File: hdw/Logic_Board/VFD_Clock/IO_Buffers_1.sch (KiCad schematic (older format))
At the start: 42 parts

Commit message: Resurrected project
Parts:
- removed R? (x16): 100, Resistors_SMD:R_0603, symbol Custom_Library:R_Custom
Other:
- note added: "Switch to nexperia QFN line driver"

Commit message: Power supply additions
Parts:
- removed R? (x16): 10K, Resistors_SMD:R_0603, symbol Custom_Library:R_Custom
- removed U? (x2): 74HCT541, Housings_SSOP:TSSOP-20_4.4x6.5mm_Pitch0.65mm, symbol 74xx:74HCT541
- added RN? (x2): 10k, Resistors_SMD:R_Array_Convex_8x0602, symbol Device:R_Pack08
- added U? (x2): 74VHC541, Package_DFN_QFN:Texas_S-PWQFN-N20, symbol Custom_Library:74VHC541
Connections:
- wire segments 84 -> 118
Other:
- note removed: "Switch to nexperia QFN line driver"

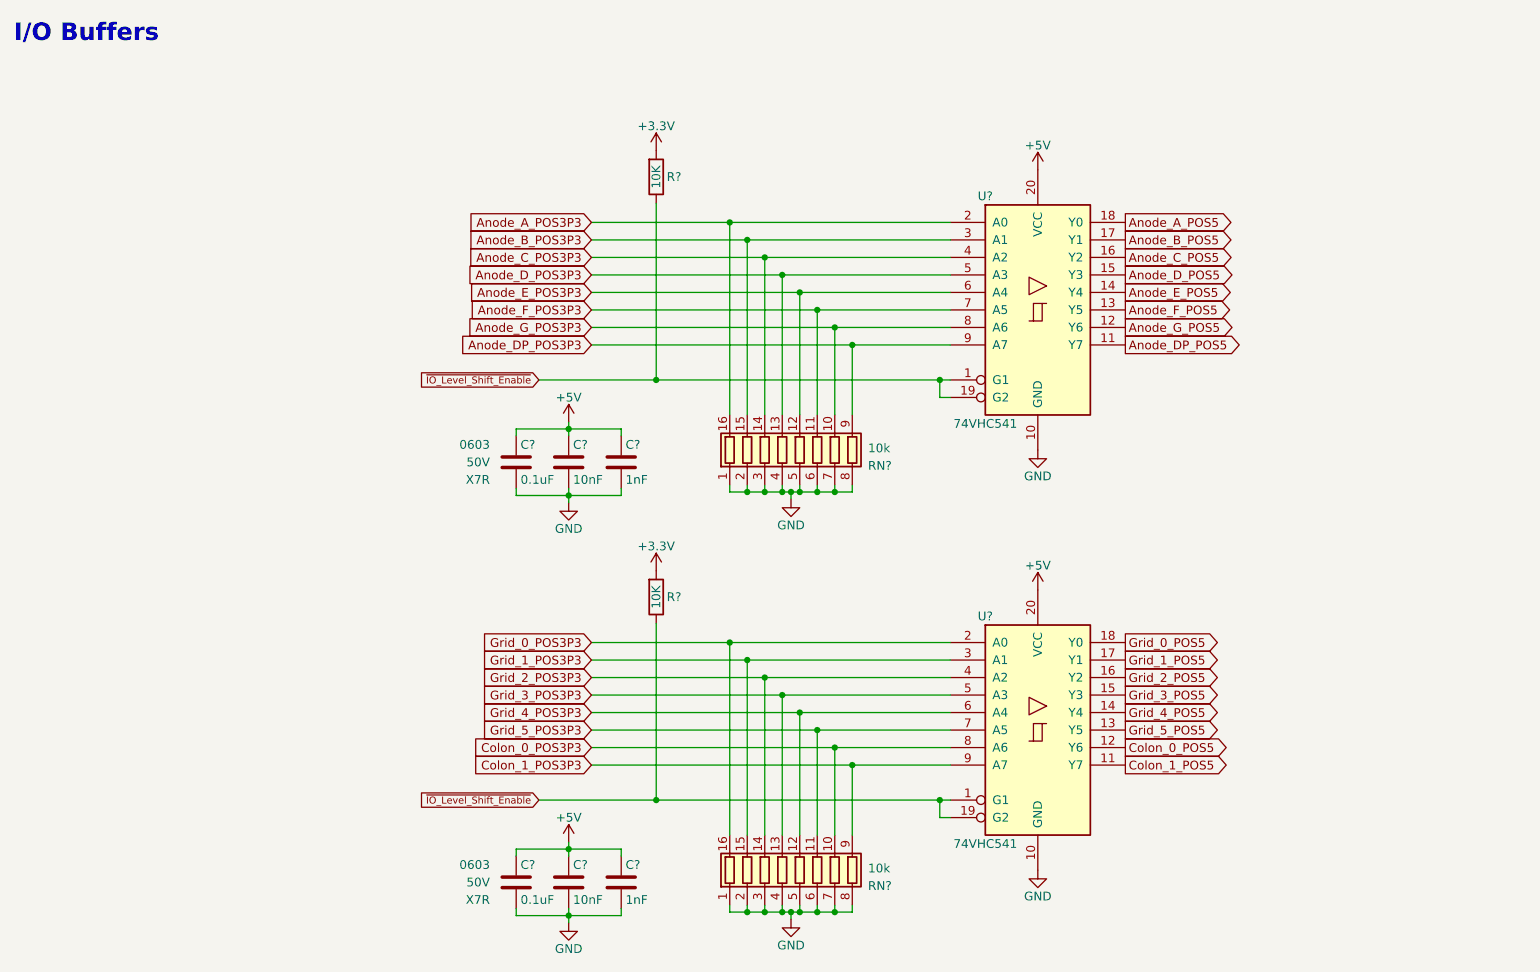
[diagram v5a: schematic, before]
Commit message: Started IV-6 display board, continued logic board development
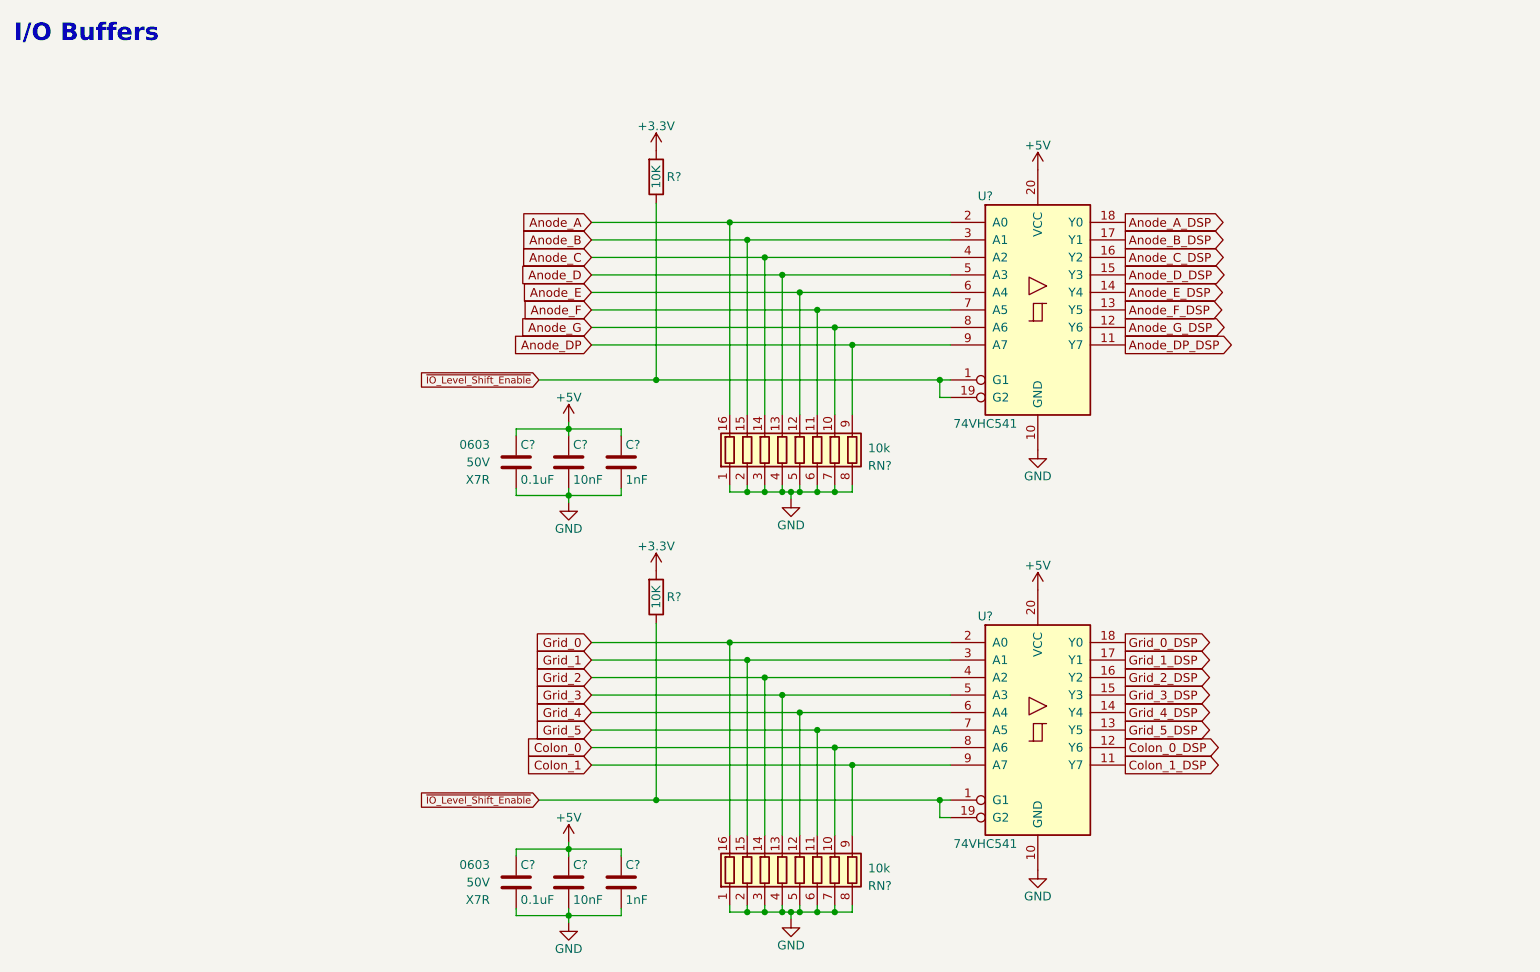
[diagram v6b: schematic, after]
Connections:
- net Anode_A_POS3P3 renamed Anode_A
- net Anode_A_POS5 renamed Anode_A_DSP
- net Anode_B_POS3P3 renamed Anode_B
- net Anode_B_POS5 renamed Anode_B_DSP
- net Anode_C_POS3P3 renamed Anode_C
- net Anode_C_POS5 renamed Anode_C_DSP
- net Anode_DP_POS3P3 renamed Anode_DP
- net Anode_DP_POS5 renamed Anode_DP_DSP
- net Anode_D_POS3P3 renamed Anode_D
- net Anode_D_POS5 renamed Anode_D_DSP
- net Anode_E_POS3P3 renamed Anode_E
- net Anode_E_POS5 renamed Anode_E_DSP
- net Anode_F_POS3P3 renamed Anode_F
- net Anode_F_POS5 renamed Anode_F_DSP
- net Anode_G_POS3P3 renamed Anode_G
- net Anode_G_POS5 renamed Anode_G_DSP
- net Colon_0_POS3P3 renamed Colon_0
- net Colon_0_POS5 renamed Colon_0_DSP
- net Colon_1_POS3P3 renamed Colon_1
- net Colon_1_POS5 renamed Colon_1_DSP
- net Grid_0_POS3P3 renamed Grid_0
- net Grid_0_POS5 renamed Grid_0_DSP
- net Grid_1_POS3P3 renamed Grid_1
- net Grid_1_POS5 renamed Grid_1_DSP
- net Grid_2_POS3P3 renamed Grid_2
- net Grid_2_POS5 renamed Grid_2_DSP
- net Grid_3_POS3P3 renamed Grid_3
- net Grid_3_POS5 renamed Grid_3_DSP
- net Grid_4_POS3P3 renamed Grid_4
- net Grid_4_POS5 renamed Grid_4_DSP
- net Grid_5_POS3P3 renamed Grid_5
- net Grid_5_POS5 renamed Grid_5_DSP
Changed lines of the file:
@@
 Connection ~ 5840 5020
 Text GLabel 3850 1720 0    50   Input ~ 0
-Anode_A_POS3P3
+Anode_A
 Text GLabel 3850 1820 0    50   Input ~ 0
-Anode_B_POS3P3
+Anode_B
 Text GLabel 3850 1920 0    50   Input ~ 0
-Anode_C_POS3P3
+Anode_C
 Text GLabel 3850 2020 0    50   Input ~ 0
-Anode_D_POS3P3
+Anode_D
 Text GLabel 3850 2120 0    50   Input ~ 0
-Anode_E_POS3P3
+Anode_E
 Text GLabel 3850 2220 0    50   Input ~ 0
-Anode_F_POS3P3
+Anode_F
 Text GLabel 3850 2320 0    50   Input ~ 0
-Anode_G_POS3P3
+Anode_G
 Text GLabel 3850 2420 0    50   Input ~ 0
-Anode_DP_POS3P3
+Anode_DP
 Text GLabel 3850 4120 0    50   Input ~ 0
-Grid_0_POS3P3
+Grid_0
 Text GLabel 3850 4220 0    50   Input ~ 0
-Grid_1_POS3P3
+Grid_1
 Text GLabel 3850 4320 0    50   Input ~ 0
-Grid_2_POS3P3
+Grid_2
 Text GLabel 3850 4420 0    50   Input ~ 0
-Grid_3_POS3P3
+Grid_3
 Text GLabel 3850 4520 0    50   Input ~ 0
-Grid_4_POS3P3
+Grid_4
 Text GLabel 3850 4620 0    50   Input ~ 0
-Grid_5_POS3P3
+Grid_5
 Text GLabel 3850 4720 0    50   Input ~ 0
-Colon_0_POS3P3
+Colon_0
 Text GLabel 3850 4820 0    50   Input ~ 0
-Colon_1_POS3P3
+Colon_1
 Text GLabel 3550 2620 0    40   Input ~ 0
 ~IO_Level_Shift_Enable
@@
 Connection ~ 4220 5020
 Text GLabel 6900 1720 2    50   Output ~ 0
-Anode_A_POS5
+Anode_A_DSP
 Text GLabel 6900 1820 2    50   Output ~ 0
-Anode_B_POS5
+Anode_B_DSP
 Text GLabel 6900 1920 2    50   Output ~ 0
-Anode_C_POS5
+Anode_C_DSP
 Text GLabel 6900 2020 2    50   Output ~ 0
-Anode_D_POS5
+Anode_D_DSP
 Text GLabel 6900 2120 2    50   Output ~ 0
-Anode_E_POS5
+Anode_E_DSP
 Text GLabel 6900 2220 2    50   Output ~ 0
-Anode_F_POS5
+Anode_F_DSP
 Text GLabel 6900 2320 2    50   Output ~ 0
-Anode_G_POS5
+Anode_G_DSP
 Text GLabel 6900 2420 2    50   Output ~ 0
-Anode_DP_POS5
+Anode_DP_DSP
 Text GLabel 6900 4120 2    50   Output ~ 0
-Grid_0_POS5
+Grid_0_DSP
 Text GLabel 6900 4220 2    50   Output ~ 0
-Grid_1_POS5
+Grid_1_DSP
 Text GLabel 6900 4320 2    50   Output ~ 0
-Grid_2_POS5
+Grid_2_DSP
 Text GLabel 6900 4420 2    50   Output ~ 0
-Grid_3_POS5
+Grid_3_DSP
 Text GLabel 6900 4520 2    50   Output ~ 0
-Grid_4_POS5
+Grid_4_DSP
 Text GLabel 6900 4620 2    50   Output ~ 0
-Grid_5_POS5
+Grid_5_DSP
 Text GLabel 6900 4720 2    50   Output ~ 0
-Colon_0_POS5
+Colon_0_DSP
 Text GLabel 6900 4820 2    50   Output ~ 0
-Colon_1_POS5
+Colon_1_DSP
 $Comp
 L Custom_Library:74VHC541 U?
